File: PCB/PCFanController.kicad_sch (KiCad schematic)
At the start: 36 parts, among them J1 Conn_01x03_Socket, J2 Conn_01x03_Socket, J3 USB_C_Receptacle_USB2.0_16P, M1 Fan_4pin, Q1 BSS138, SW1 SW_Push, SW2 SW_Push, SW3 SW_Push, U1 ATtiny404-SS, U2 74HC595, U3 74HC595, U4 OSL40562-LR, U5 AP63203WU, U6 CH221K

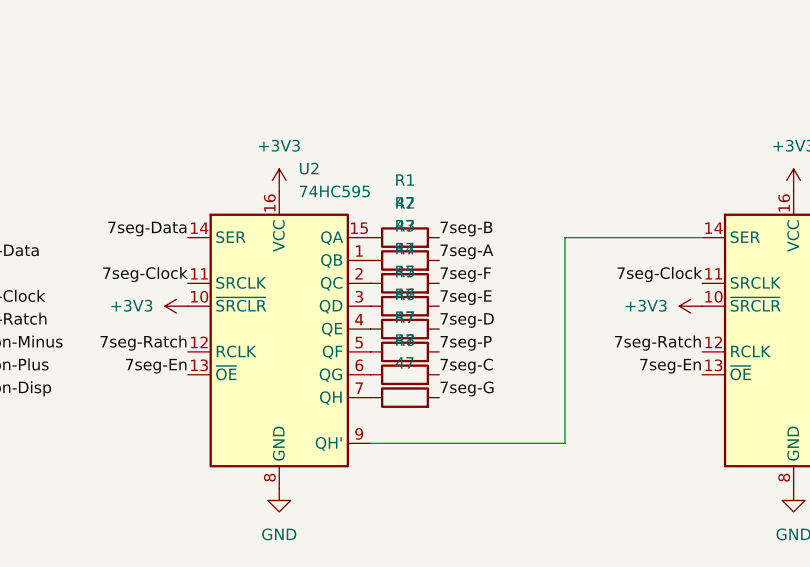
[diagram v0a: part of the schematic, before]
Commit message: 抵抗値修正
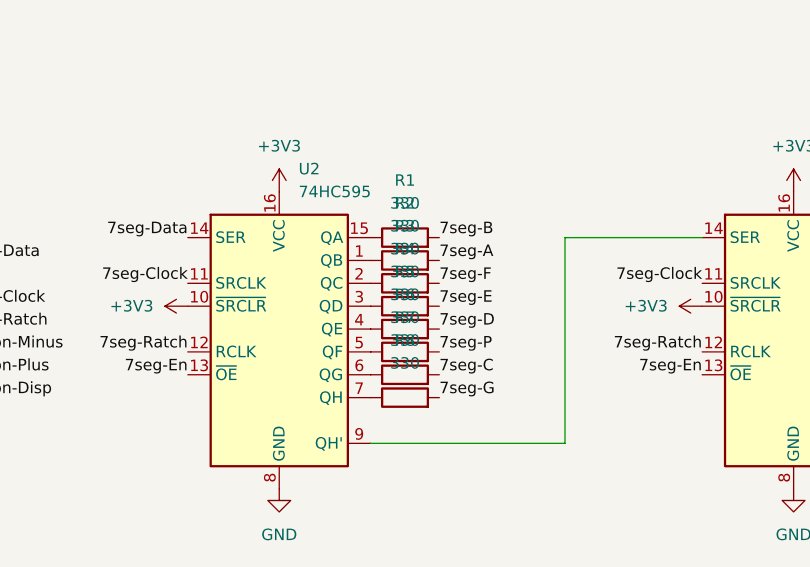
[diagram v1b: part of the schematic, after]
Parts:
- R1, R2, R3, R4, R5, R6, R7, R8: value 47 -> 330
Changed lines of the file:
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@@
 			)
 		)
-		(property "Value" "47"
+		(property "Value" "330"
 			(at 102.87 54.61 90)
 			(show_name no)
@@
 			)
 		)
-		(property "Value" "47"
+		(property "Value" "330"
 			(at 102.87 49.53 90)
 			(show_name no)
@@
 			)
 		)
-		(property "Value" "47"
+		(property "Value" "330"
 			(at 102.87 59.69 90)
 			(show_name no)
@@
 			)
 		)
-		(property "Value" "47"
+		(property "Value" "330"
 			(at 102.87 62.23 90)
 			(show_name no)
@@
 			)
 		)
-		(property "Value" "47"
+		(property "Value" "330"
 			(at 102.87 52.07 90)
 			(show_name no)
@@
 			)
 		)
-		(property "Value" "47"
+		(property "Value" "330"
 			(at 102.87 67.31 90)
 			(show_name no)
@@
 			)
 		)
-		(property "Value" "47"
+		(property "Value" "330"
 			(at 102.87 64.77 90)
 			(show_name no)
@@
 			)
 		)
-		(property "Value" "47"
+		(property "Value" "330"
 			(at 102.87 57.15 90)
 			(show_name no)

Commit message: ベタはがした、MOSFET貼った
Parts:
- added Q2: MTN2306AN3, Package_TO_SOT_SMD:SOT-23, symbol Transistor_FET:BSS138
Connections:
- net GND: now also Q2.2 (S); no longer M1.1 (-)
- net Fan-Gate: now reaches U3.1 (QB)
- net Fan-Gate: now also Q2.1 (G)
- new net Fan-Gnd: M1.1 (-), Q2.3 (D)
- no-connect marks 13 -> 12
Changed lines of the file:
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@@
 	)
 	(no_connect
-		(at 156.21 55.88)
-	)
-	(no_connect
 		(at 156.21 60.96)
 	)
@@
 	(wire
 		(pts
+			(xy 187.96 55.88) (xy 187.96 74.93)
+		)
+		(stroke
+			(width 0)
+			(type default)
+		)
+	)
+	(wire
+		(pts
 			(xy 116.84 118.11) (xy 116.84 123.19)
 		)
@@
 	(wire
 		(pts
+			(xy 199.39 74.93) (xy 199.39 82.55)
+		)
+		(stroke
+			(width 0)
+			(type default)
+		)
+	)
+	(wire
+		(pts
 			(xy 137.16 118.11) (xy 144.78 118.11)
 		)
@@
 	(wire
 		(pts
+			(xy 177.8 55.88) (xy 187.96 55.88)
+		)
+		(stroke
+			(width 0)
+			(type default)
+		)
+	)
+	(wire
+		(pts
 			(xy 152.4 126.365) (xy 144.78 126.365)
 		)
@@
 	(wire
 		(pts
+			(xy 187.96 74.93) (xy 199.39 74.93)
+		)
+		(stroke
+			(width 0)
+			(type default)
+		)
+	)
+	(wire
+		(pts
 			(xy 62.23 119.38) (xy 62.23 121.92)
 		)
@@
 		)
 	)
+	(label "Fan-Gnd"
+		(at 187.96 55.88 180)
+		(effects
+			(font
+				(size 1.27 1.27)
+			)
+			(justify right bottom)
+		)
+	)
 	(label "Button-Plus"
 		(at 223.52 120.65 180)
@@
 		)
 	)
+	(label "Fan-Gate"
+		(at 191.77 87.63 180)
+		(effects
+			(font
+				(size 1.27 1.27)
+			)
+			(justify right bottom)
+		)
+	)
 	(label "7seg-1"
 		(at 156.21 68.58 0)
@@
 		)
 	)
+	(label "Fan-Gate"
+		(at 156.21 55.88 0)
+		(effects
+			(font
+				(size 1.27 1.27)
+			)
+			(justify left bottom)
+		)
+	)
 	(label "7seg-D"
 		(at 200.66 63.5 180)
@@
 	(symbol
 		(lib_id "power:GND")
-		(at 177.8 55.88 0)
+		(at 30.48 45.72 270)
 		(unit 1)
 		(body_style 1)
@@
 		(dnp no)
 		(fields_autoplaced yes)
-		(property "Reference" "#PWR010"
-			(at 177.8 62.23 0)
+		(property "Reference" "#PWR06"
+			(at 24.13 45.72 0)
 			(hide yes)
 			(show_name no)
@@
 		)
 		(property "Value" "GND"
-			(at 177.8 60.96 0)
+			(at 26.67 45.7199 90)
 			(show_name no)
 			(do_not_autoplace no)
@@
 					(size 1.27 1.27)
 				)
+				(justify right)
 			)
 		)
 		(property "Footprint" ""
-			(at 177.8 55.88 0)
+			(at 30.48 45.72 0)
 			(hide yes)
 			(show_name no)
@@
 		)
 		(property "Datasheet" ""
-			(at 177.8 55.88 0)
+			(at 30.48 45.72 0)
 			(hide yes)
 			(show_name no)
@@
 		)
 		(property "Description" "Power symbol creates a global label with name \"GND\" , ground"
-			(at 177.8 55.88 0)
+			(at 30.48 45.72 0)
 			(hide yes)
 			(show_name no)
@@
 			(project "PCFanController"
 				(path "/52b4d307-cc39-4fe2-86bc-cae0e5ee7f53"
-					(reference "#PWR010")
+					(reference "#PWR06")
 					(unit 1)
 				)
@@
 	(symbol
 		(lib_id "power:GND")
-		(at 30.48 45.72 270)
+		(at 199.39 92.71 0)
 		(unit 1)
 		(body_style 1)
@@
 		(dnp no)
 		(fields_autoplaced yes)
-		(property "Reference" "#PWR06"
-			(at 24.13 45.72 0)
+		(property "Reference" "#PWR016"
+			(at 199.39 99.06 0)
 			(hide yes)
 			(show_name no)
@@
 		)
 		(property "Value" "GND"
-			(at 26.67 45.7199 90)
+			(at 199.39 97.79 0)
 			(show_name no)
 			(do_not_autoplace no)
@@
 					(size 1.27 1.27)
 				)
-				(justify right)
 			)
 		)
 		(property "Footprint" ""
-			(at 30.48 45.72 0)
+			(at 199.39 92.71 0)
 			(hide yes)
 			(show_name no)
@@
 		)
 		(property "Datasheet" ""
-			(at 30.48 45.72 0)
+			(at 199.39 92.71 0)
 			(hide yes)
 			(show_name no)
@@
 		)
 		(property "Description" "Power symbol creates a global label with name \"GND\" , ground"
-			(at 30.48 45.72 0)
+			(at 199.39 92.71 0)
 			(hide yes)
 			(show_name no)
@@
 			(project "PCFanController"
 				(path "/52b4d307-cc39-4fe2-86bc-cae0e5ee7f53"
-					(reference "#PWR06")
+					(reference "#PWR016")
 					(unit 1)
 				)
@@
 		(dnp no)
 		(fields_autoplaced yes)
-		(property "Reference" "#PWR012"
+		(property "Reference" "#PWR011"
 			(at 139.7 60.96 0)
 			(hide yes)
@@
 			(project "PCFanController"
 				(path "/52b4d307-cc39-4fe2-86bc-cae0e5ee7f53"
-					(reference "#PWR012")
+					(reference "#PWR011")
 					(unit 1)
 				)
@@
 		(dnp no)
 		(fields_autoplaced yes)
-		(property "Reference" "#PWR015"
+		(property "Reference" "#PWR014"
 			(at 146.05 87.63 0)
 			(hide yes)
@@
 			(project "PCFanController"
 				(path "/52b4d307-cc39-4fe2-86bc-cae0e5ee7f53"
-					(reference "#PWR015")
+					(reference "#PWR014")
 					(unit 1)
 				)
@@
 		(dnp no)
 		(fields_autoplaced yes)
-		(property "Reference" "#PWR014"
+		(property "Reference" "#PWR013"
 			(at 88.9 87.63 0)
 			(hide yes)
@@
 			(project "PCFanController"
 				(path "/52b4d307-cc39-4fe2-86bc-cae0e5ee7f53"
-					(reference "#PWR014")
+					(reference "#PWR013")
 					(unit 1)
 				)
@@
 		(dnp no)
 		(fields_autoplaced yes)
-		(property "Reference" "#PWR016"
+		(property "Reference" "#PWR015"
 			(at 180.34 87.63 0)
 			(hide yes)
@@
 			(project "PCFanController"
 				(path "/52b4d307-cc39-4fe2-86bc-cae0e5ee7f53"
-					(reference "#PWR016")
+					(reference "#PWR015")
 					(unit 1)
 				)
@@
 		(dnp no)
 		(fields_autoplaced yes)
-		(property "Reference" "#PWR011"
+		(property "Reference" "#PWR010"
 			(at 82.55 60.96 0)
 			(hide yes)
@@
 			(project "PCFanController"
 				(path "/52b4d307-cc39-4fe2-86bc-cae0e5ee7f53"
-					(reference "#PWR011")
+					(reference "#PWR010")
 					(unit 1)
 				)
@@
 		(dnp no)
 		(fields_autoplaced yes)
-		(property "Reference" "#PWR013"
+		(property "Reference" "#PWR012"
 			(at 38.1 87.63 0)
 			(hide yes)
@@
 			(project "PCFanController"
 				(path "/52b4d307-cc39-4fe2-86bc-cae0e5ee7f53"
-					(reference "#PWR013")
+					(reference "#PWR012")
 					(unit 1)
 				)
@@
 					(unit 1)
 				)
+			)
+		)
+	)
+	(symbol
+		(lib_id "Transistor_FET:BSS138")
+		(at 196.85 87.63 0)
+		(unit 1)
+		(body_style 1)
+		(exclude_from_sim no)
+		(in_bom yes)
+		(on_board yes)
+		(in_pos_files yes)
+		(dnp no)
+		(fields_autoplaced yes)
+		(property "Reference" "Q2"
+			(at 203.2 86.3599 0)
+			(show_name no)
+			(do_not_autoplace no)
+			(effects
+				(font
+					(size 1.27 1.27)
+				)
+				(justify left)
+			)
+		)
+		(property "Value" "MTN2306AN3"
+			(at 203.2 88.8999 0)
+			(show_name no)
+			(do_not_autoplace no)
+			(effects
+				(font
+					(size 1.27 1.27)
+				)
+				(justify left)
+			)
+		)
+		(property "Footprint" "Package_TO_SOT_SMD:SOT-23"
+			(at 201.93 89.535 0)
+			(hide yes)
+			(show_name no)
+			(do_not_autoplace no)
+			(effects
+				(font
+					(size 1.27 1.27)
+					(italic yes)
+				)
+				(justify left)
+			)
+		)
+		(property "Datasheet" "https://www.onsemi.com/pub/Collateral/BSS138-D.PDF"
+			(at 201.93 91.44 0)
+			(hide yes)
+			(show_name no)
+			(do_not_autoplace no)
+			(effects
+				(font
+					(size 1.27 1.27)
+				)
+				(justify left)
+			)
+		)
+		(property "Description" "50V Vds, 0.22A Id, N-Channel MOSFET, SOT-23"
+			(at 196.85 87.63 0)
+			(hide yes)
+			(show_name no)
+			(do_not_autoplace no)
+			(effects
+				(font
+					(size 1.27 1.27)
+				)
+			)
+		)
+		(pin "1"
+		)
+		(pin "2"
+		)
+		(pin "3"
+		)
+		(instances
+			(project "PCFanController"
+				(path "/52b4d307-cc39-4fe2-86bc-cae0e5ee7f53"
+					(reference "Q2")
+					(unit 1)
+				)

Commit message: VBus表に、桁選択からENを外し
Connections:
- net 7seg-En: no longer U3.13 (~{OE})
- net GND: now also U3.13 (~{OE})
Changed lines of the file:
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@@
 		)
 	)
-	(label "7seg-En"
-		(at 135.89 68.58 180)
-		(effects
-			(font
-				(size 1.27 1.27)
-			)
-			(justify right bottom)
-		)
-	)
 	(label "7seg-E"
 		(at 106.68 60.96 0)
@@
 					(unit 1)
 				)
+			)
+		)
+	)
+	(symbol
+		(lib_id "power:GND")
+		(at 135.89 68.58 270)
+		(unit 1)
+		(body_style 1)
+		(exclude_from_sim no)
+		(in_bom yes)
+		(on_board yes)
+		(in_pos_files yes)
+		(dnp no)
+		(fields_autoplaced yes)
+		(property "Reference" "#PWR032"
+			(at 129.54 68.58 0)
+			(hide yes)
+			(show_name no)
+			(do_not_autoplace no)
+			(effects
+				(font
+					(size 1.27 1.27)
+				)
+			)
+		)
+		(property "Value" "GND"
+			(at 132.08 68.5799 90)
+			(show_name no)
+			(do_not_autoplace no)
+			(effects
+				(font
+					(size 1.27 1.27)
+				)
+				(justify right)
+			)
+		)
+		(property "Footprint" ""
+			(at 135.89 68.58 0)
+			(hide yes)
+			(show_name no)
+			(do_not_autoplace no)
+			(effects
+				(font
+					(size 1.27 1.27)
+				)
+			)
+		)
+		(property "Datasheet" ""
+			(at 135.89 68.58 0)
+			(hide yes)
+			(show_name no)
+			(do_not_autoplace no)
+			(effects
+				(font
+					(size 1.27 1.27)
+				)
+			)
+		)
+		(property "Description" "Power symbol creates a global label with name \"GND\" , ground"
+			(at 135.89 68.58 0)
+			(hide yes)
+			(show_name no)
+			(do_not_autoplace no)
+			(effects
+				(font
+					(size 1.27 1.27)
+				)
+			)
+		)
+		(pin "1"
+		)
+		(instances
+			(project "PCFanController"
+				(path "/52b4d307-cc39-4fe2-86bc-cae0e5ee7f53"
+					(reference "#PWR032")
+					(unit 1)
+				)

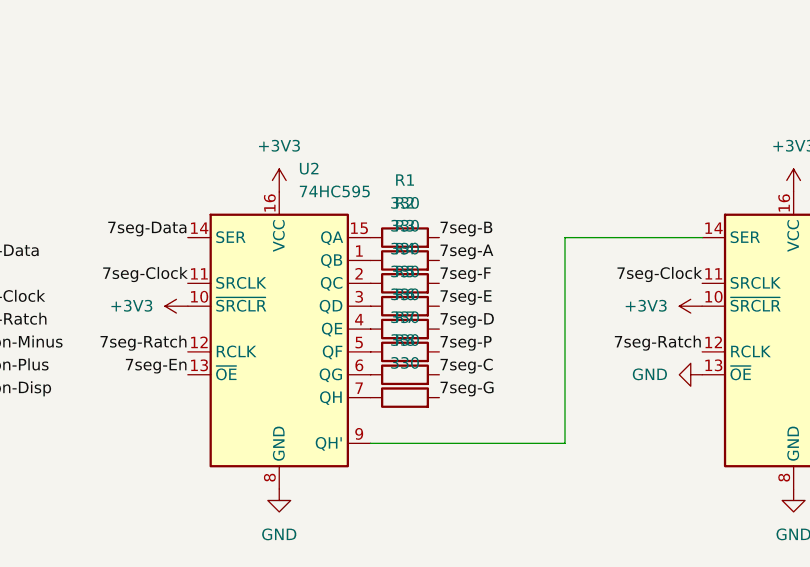
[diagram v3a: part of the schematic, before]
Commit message: 抵抗値変更
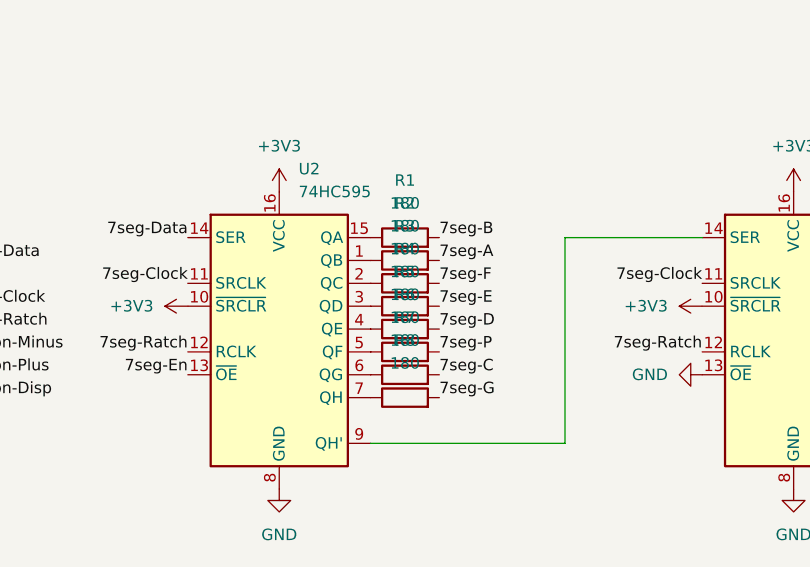
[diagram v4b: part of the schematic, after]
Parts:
- R1, R2, R3, R4, R5, R6, R7, R8: value 330 -> 180
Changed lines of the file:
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@@
 			)
 		)
-		(property "Value" "330"
+		(property "Value" "180"
 			(at 102.87 54.61 90)
 			(show_name no)
@@
 			)
 		)
-		(property "Value" "330"
+		(property "Value" "180"
 			(at 102.87 49.53 90)
 			(show_name no)
@@
 			)
 		)
-		(property "Value" "330"
+		(property "Value" "180"
 			(at 102.87 59.69 90)
 			(show_name no)
@@
 			)
 		)
-		(property "Value" "330"
+		(property "Value" "180"
 			(at 102.87 62.23 90)
 			(show_name no)
@@
 			)
 		)
-		(property "Value" "330"
+		(property "Value" "180"
 			(at 102.87 52.07 90)
 			(show_name no)
@@
 			)
 		)
-		(property "Value" "330"
+		(property "Value" "180"
 			(at 102.87 67.31 90)
 			(show_name no)
@@
 			)
 		)
-		(property "Value" "330"
+		(property "Value" "180"
 			(at 102.87 64.77 90)
 			(show_name no)
@@
 			)
 		)
-		(property "Value" "330"
+		(property "Value" "180"
 			(at 102.87 57.15 90)
 			(show_name no)

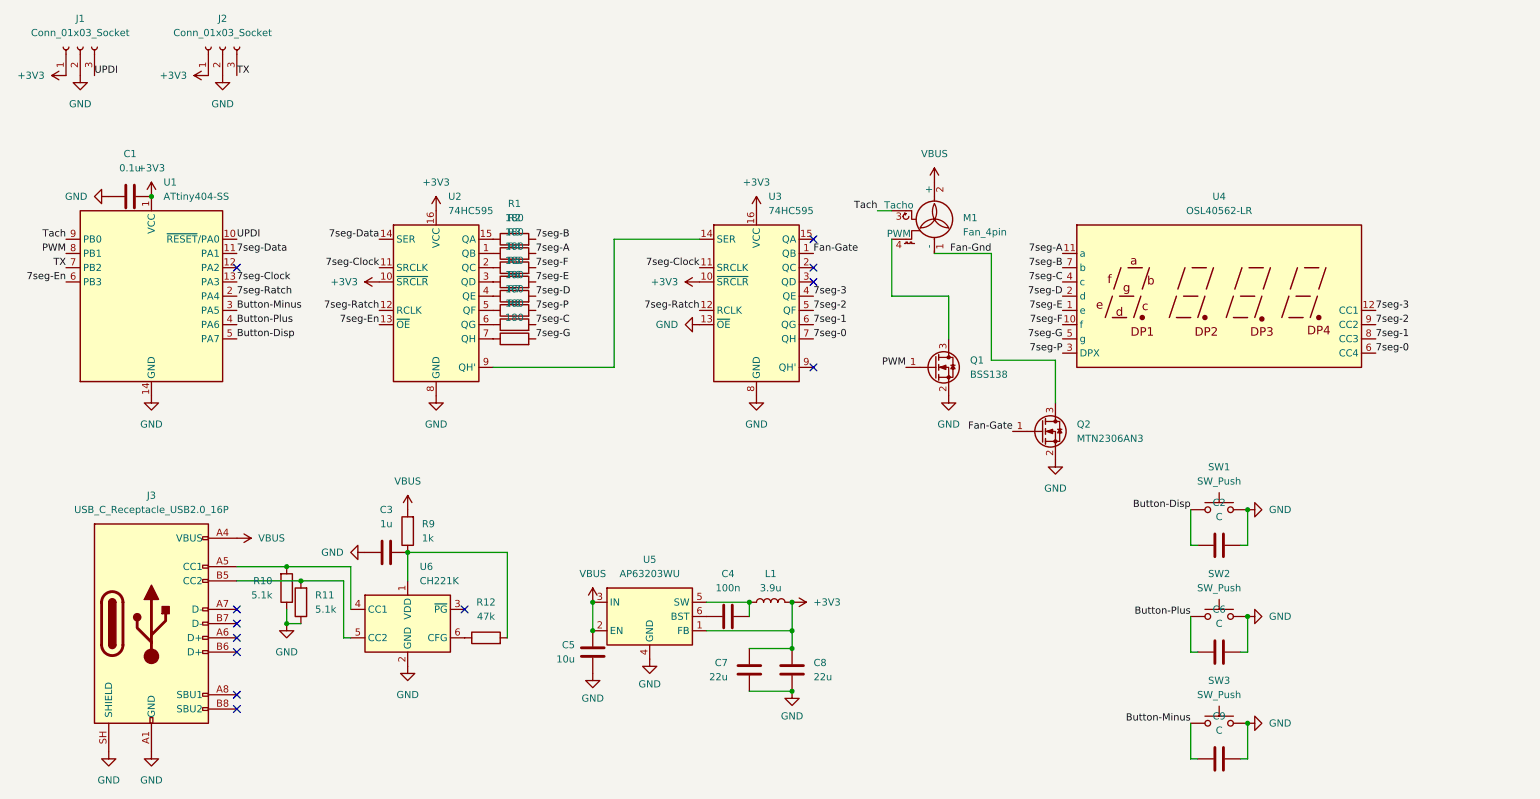
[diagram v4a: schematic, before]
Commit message: 未実装を明示
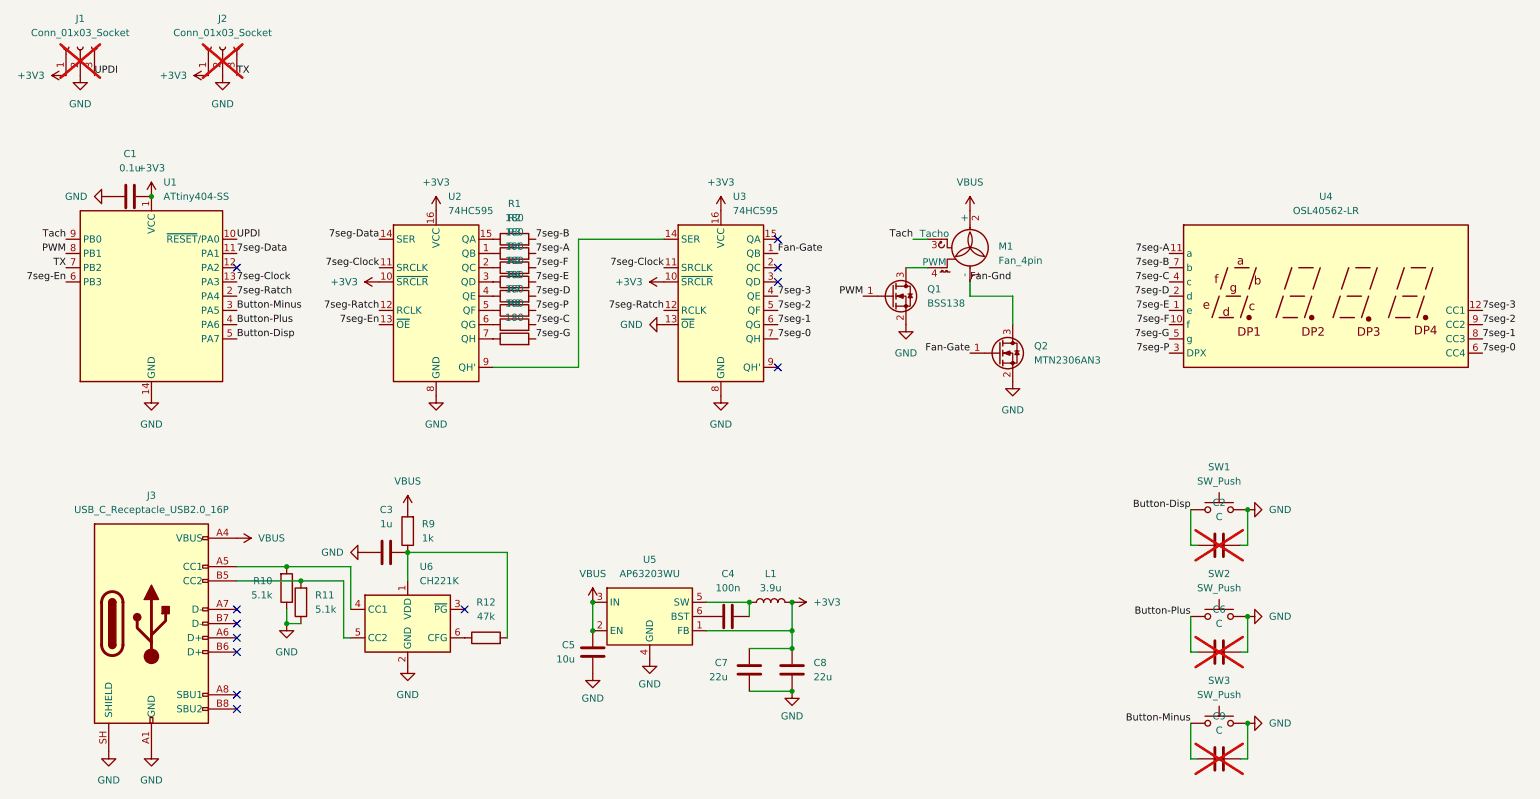
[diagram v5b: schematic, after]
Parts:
- C2, C6, C9, J1, J2: now not fitted
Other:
- moved on the sheet: M1, Q1, Q2, U3, U4
